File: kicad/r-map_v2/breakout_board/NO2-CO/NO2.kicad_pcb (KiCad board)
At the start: 2 copper layers, 33 x 28.6 mm, 29 parts, among them P1 CONN_01X05, P2 CONN_01X05, Q1 2N7002, Q2 2N7002, Q3 2N7002, Q4 2N7002, Q5 2N7002, Q6 2N7002, Q7 BC849, Q8 BC849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

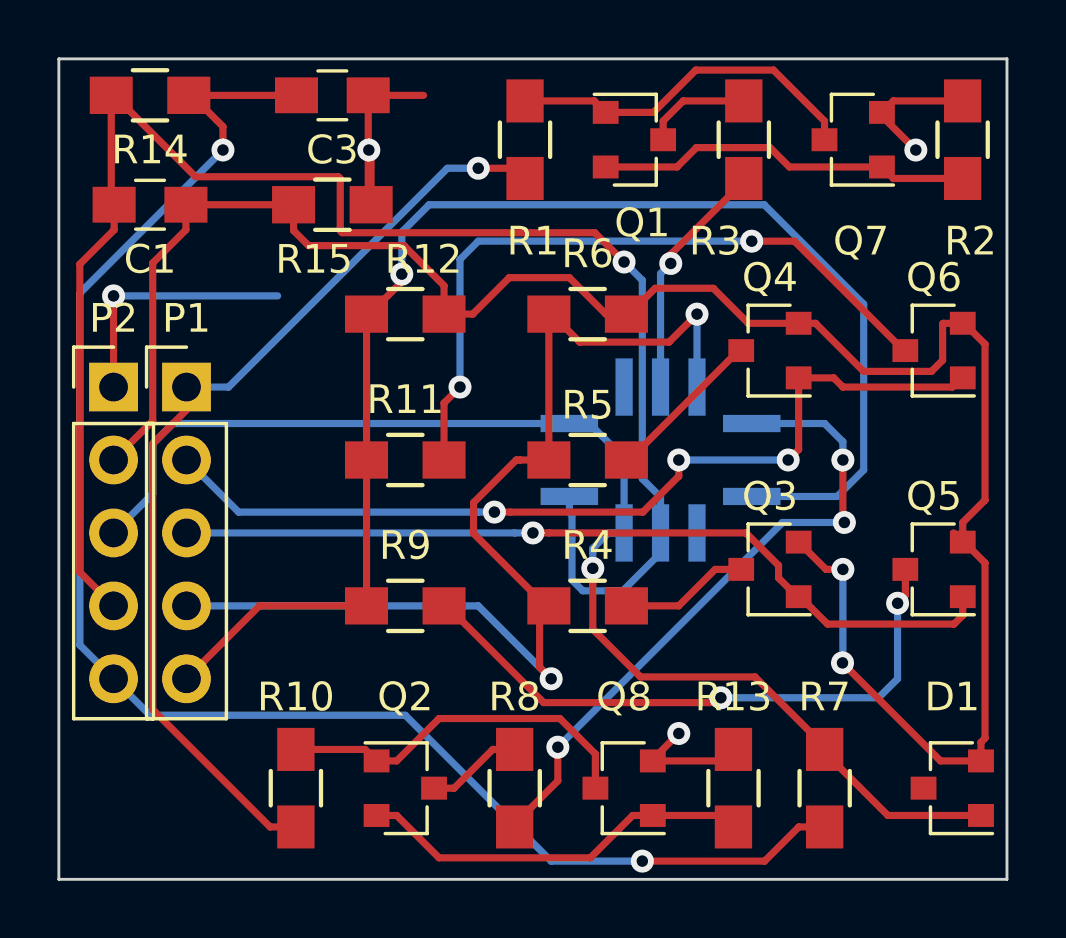
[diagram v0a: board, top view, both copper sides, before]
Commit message: Board correction for MICS-4514 bad pinout. Correction for Stima_AirQuality_Connector connector pinout
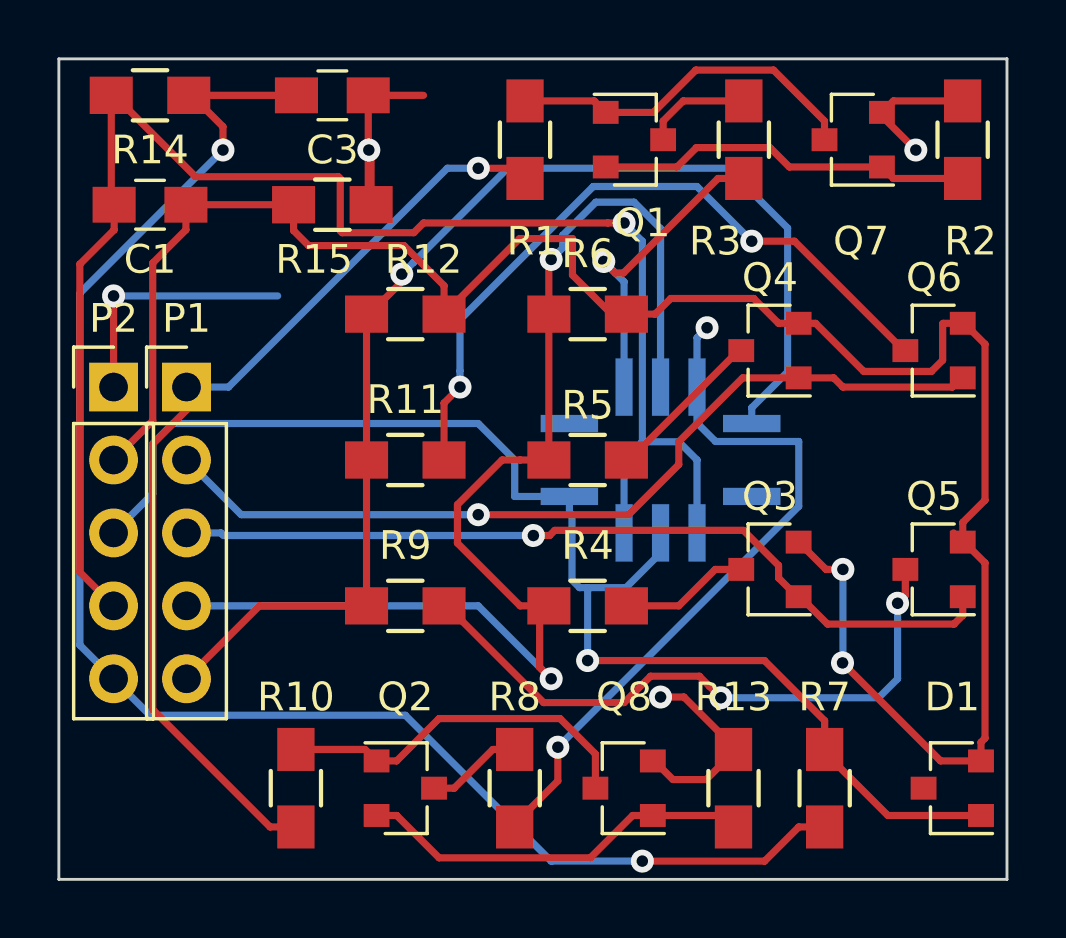
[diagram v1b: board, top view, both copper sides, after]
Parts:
- R13: value R -> 17R4
- R2: value R -> 21R5
- R8: value 50 -> 47
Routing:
- net NO2: track 48.9 -> 42.6 mm
- net CO: track 38.2 -> 43.7 mm
- net VREF: track 43.9 -> 46.8 mm
- net GND: track 25.7 -> 28.3 mm
- net Net-(R3-Pad1): track 8.47 -> 11.1 mm
- net Net-(R8-Pad1): track 22.9 -> 24.8 mm, vias 3 -> 2
- net VDD: track 57.5 -> 55.9 mm
- net GNDD: track 71.9 -> 73.5 mm
- net SCALE_1: track 31.8 -> 30.5 mm, vias 3 -> 1
- net Net-(Q5-Pad3): track 21.5 -> 22.1 mm
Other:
- board text added: "Ver 2"
